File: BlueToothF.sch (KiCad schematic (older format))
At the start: 1 part, among them P1 CONN_01X4

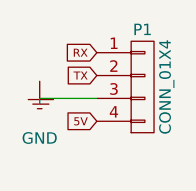
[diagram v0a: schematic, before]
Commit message: added TPS61222DCK boost converter
-added TPS61222DCK boost converter for 5V input of the encoder
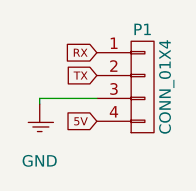
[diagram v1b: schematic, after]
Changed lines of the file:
@@
 L GND #PWR46
 U 1 1 597FE6B7
-P 4800 2900
-F 0 "#PWR46" H 4800 2650 50  0001 C CNN
-F 1 "GND" H 4800 2750 50  0000 C CNN
-F 2 "" H 4800 2900 50  0001 C CNN
-F 3 "" H 4800 2900 50  0001 C CNN
-	1    4800 2900
+P 4800 3000
+F 0 "#PWR46" H 4800 2750 50  0001 C CNN
+F 1 "GND" H 4800 2850 50  0000 C CNN
+F 2 "" H 4800 3000 50  0001 C CNN
+F 3 "" H 4800 3000 50  0001 C CNN
+	1    4800 3000
 	1    0    0    -1
 $EndComp

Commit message: Rev 1.0 done
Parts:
- P1: manf# (none) -> NONE
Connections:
- net 5V renamed MCUv
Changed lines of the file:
@@
 F 2 "Socket_Strips:Socket_Strip_Straight_1x04_Pitch2.54mm" H 5250 2425 50  0001 C CNN
 F 3 "" H 5250 2425 50  0000 C CNN
+F 4 "NONE" H 5250 3175 50  0001 C CNN "manf#"
 	1    5250 2825
 	1    0    0    -1
 $EndComp
-Text GLabel 5050 2775 0    35   Input ~ 0
-TX
-Text GLabel 5050 2975 0    35   Input ~ 0
-5V
-Text GLabel 5050 2675 0    35   Input ~ 0
-RX
 $Comp
-L GND #PWR48
+L GND #PWR52
 U 1 1 597FE6B7
 P 4800 3000
-F 0 "#PWR48" H 4800 2750 50  0001 C CNN
+F 0 "#PWR52" H 4800 2750 50  0001 C CNN
 F 1 "GND" H 4800 2850 50  0000 C CNN
 F 2 "" H 4800 3000 50  0001 C CNN
@@
 	1    0    0    -1
 $EndComp
+Text GLabel 5050 2775 0    35   Input ~ 0
+TX
+Text GLabel 5050 2975 0    35   Input ~ 0
+MCUv
+Text GLabel 5050 2675 0    35   Input ~ 0
+RX
 Wire Wire Line
 	5050 2875 4800 2875

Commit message: fixed the unconnected teensy bootloader chip
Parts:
- P1: manf# NONE -> DNP
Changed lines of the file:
@@
 F 2 "Socket_Strips:Socket_Strip_Straight_1x04_Pitch2.54mm" H 5250 2425 50  0001 C CNN
 F 3 "" H 5250 2425 50  0000 C CNN
-F 4 "NONE" H 5250 3175 50  0001 C CNN "manf#"
+F 4 "DNP" H 5250 3175 50  0001 C CNN "manf#"
 	1    5250 2825
 	1    0    0    -1
